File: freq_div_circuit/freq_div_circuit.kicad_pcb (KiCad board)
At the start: 2 copper layers, 68.6 x 53.3 mm, 18 parts, among them P1 BNC, P2 BNC, U1 TL071, U2 MAX1044, U3 MCP6021, U4 7805, U5 7905

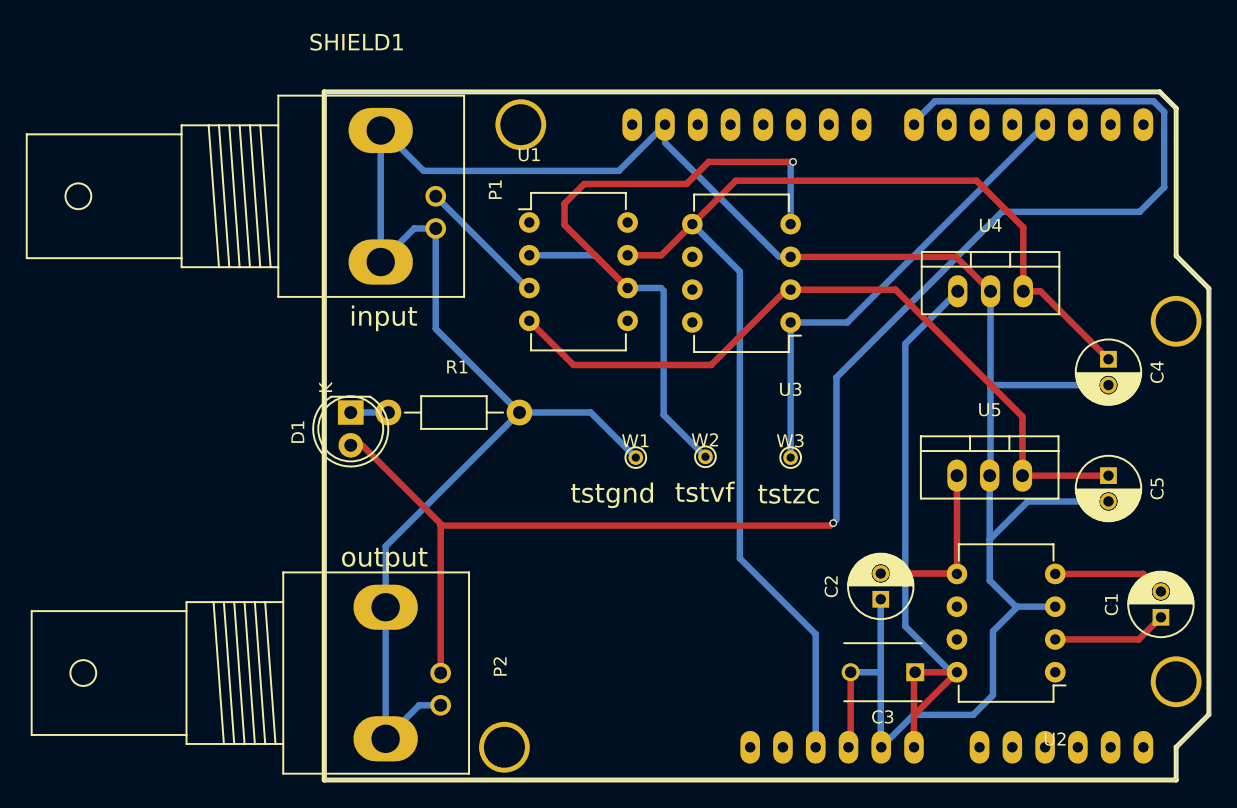
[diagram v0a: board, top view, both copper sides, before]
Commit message: updating schematic with tl071cp
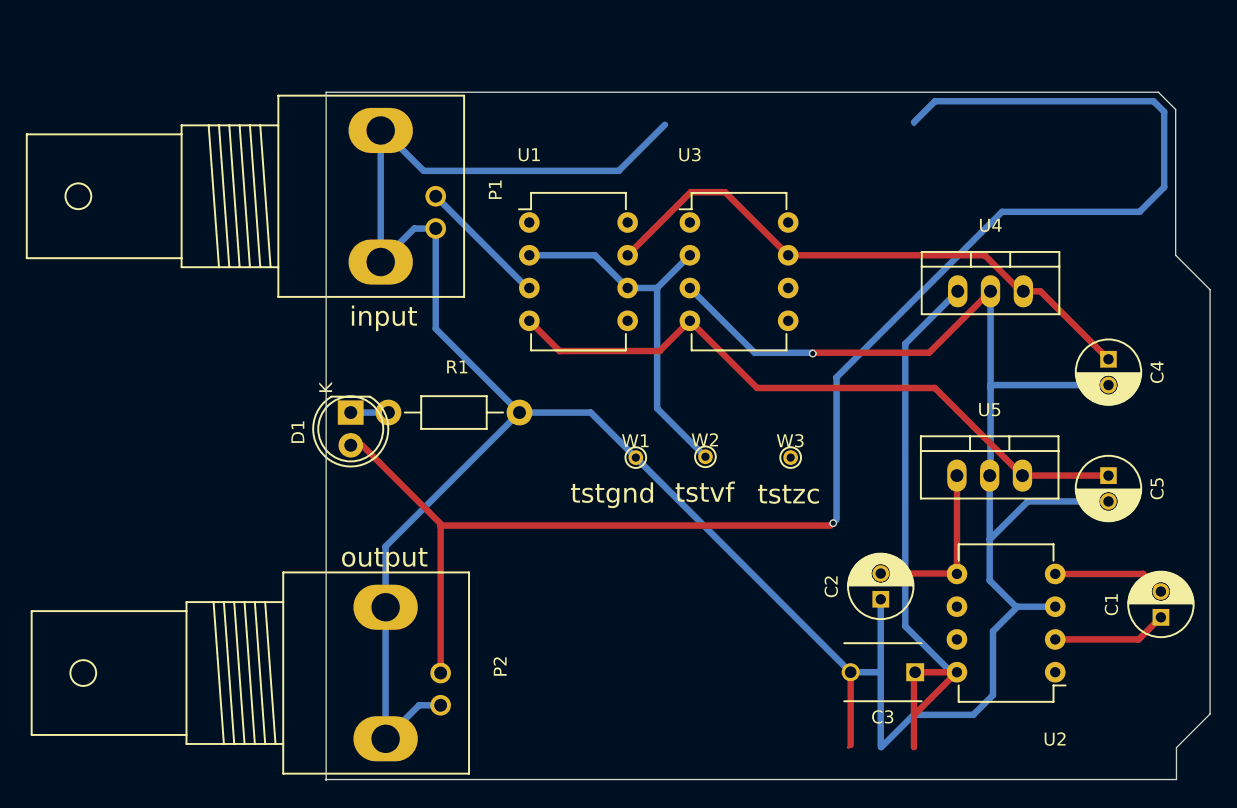
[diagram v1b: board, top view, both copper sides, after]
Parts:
- removed SHIELD1: ARDUINO_SHIELD, arduino_shields:ARDUINO SHIELD
- U3: value MCP6021 -> TL071
- moved U3 11.0 mm to (176.8, 61.8), turned to 0 degrees
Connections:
- U3 pad 1: Net-(SHIELD1-Pad3) -> (no net)
- U3 pad 2: -5V -> Net-(U1-Pad2)
- U3 pad 4: Net-(U1-Pad2) -> -5V
- U3 pad 5: +5V -> (no net)
- U3 pad 6: (no net) -> Net-(SHIELD1-Pad3)
- U3 pad 7: (no net) -> +5V
- W3 pad 1: Net-(SHIELD1-Pad3) -> Net-(W3-Pad1)
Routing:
- net +5V: track 92.8 -> 44.7 mm
- net Net-(SHIELD1-Pad3): track 36.6 -> 0.32 mm
- net Net-(U1-Pad2): track 58.3 -> 29.2 mm, vias 1 -> 0
- net GND: track 222.9 -> 242.4 mm, vias 0 -> 1
- net -5V: track 57.4 -> 51.8 mm
